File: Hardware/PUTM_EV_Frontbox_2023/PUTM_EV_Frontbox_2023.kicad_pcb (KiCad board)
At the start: 4 copper layers, 75 x 57.9 mm, 251 parts, among them IC1 ELVH-MF12D-HRRJ-C-N3A4, IC2 ELVH-MF12D-HRRJ-C-N3A4, J1 Conn_02x16_Counter_Clockwise, J2 Conn_01x04, K1 UMS05-1A80-75D, Q1 NX7002AK, SW1 Reset switch, U1 STM32G473RCTx, U10 TLP291-4, U11 TLP291-4, U12 MCP2542FDxMF, U13 MCP6001, U14 MCP6N11-005, U15 MCP6001, U16 MCP6N11-005, U17 MCP6002-xMC, U18 MCP6N11-005, U19 TLV743P, U2 MCP6002-xMC, U20 LM4040DBZ-5, U21 MCP6001, U22 MCP6N11-005, U23 MCP6001, U24 MCP6001, U25 MCP6N11-005, U26 MCP6001, U3 IMS330DHCX, U4 TLV743P, U5 TLV743P, U6 BD50FC0FP, U7 LM62440-Q1, U8 MCP2542FDxMF, U9 MCP6N11-005, Y1 ABM8G-48.000MHZ

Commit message: Changed board outline and layout to match ASB
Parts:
- removed J2: Conn_01x04, Connector_PinHeader_2.54mm:PinHeader_1x05_P2.54mm_Vertical
- removed K1: UMS05-1A80-75D, Relay_THT:Relay_StandexMeder_UMS
- added D12: D_Small, Diode_SMD:D_0805_2012Metric_Pad1.15x1.40mm_HandSolder, F.Cu at (190.9, 48.8)
- added H3: MountingHole_Pad, MountingHole:MountingHole_3.2mm_M3_DIN965_Pad_TopBottom, F.Cu at (109.8, 22.1)
- added H4: MountingHole_Pad, MountingHole:MountingHole_3.2mm_M3_DIN965_Pad_TopBottom, F.Cu at (197.8, 22.1)
- added J3: STLINK-V3MINIE, Frontbox:STLINK-V3MINIE, B.Cu at (167.2, 38.8)
- added K2: FINDER-32.21-x000, Relay_THT:Relay_SPDT_Finder_32.21-x000, F.Cu at (190.6, 51.6)
- added R52: 2k, Resistor_SMD:R_0402_1005Metric, F.Cu at (178.6, 61.4)
- added R53: 10k, Resistor_SMD:R_0402_1005Metric, F.Cu at (179.6, 71.0)
- J1: value Conn_02x16_Counter_Clockwise -> Conn_02x15_Counter_Clockwise; footprint Connector_PinHeader_2.54mm:PinHeader_2x16_P2.54mm_Vertical -> Connector_IDC:IDC-Header_2x15-1MP_P2.54mm_Latch6.5mm_Vertical
- moved R20 215.7 mm to (149.1, 71.0)
- moved R21 215.7 mm to (149.1, 69.4)
- moved TP8 215.7 mm to (144.0, 79.3)
- moved C2 215.7 mm to (146.0, 67.9)
- moved C26 215.7 mm to (150.3, 72.8)
- moved D5 215.7 mm to (148.8, 75.2)
- moved R17 215.7 mm to (146.0, 71.0)
- moved R18 215.7 mm to (146.0, 69.4)
- moved R5 215.7 mm to (146.0, 75.2)
- moved R7 215.7 mm to (146.0, 76.7)
- moved TP9 215.7 mm to (145.2, 65.2)
- moved C21 215.7 mm to (149.1, 67.9)
- moved C22 215.7 mm to (149.1, 62.9)
- moved R8 215.7 mm to (149.1, 76.7)
- moved TP6 215.7 mm to (150.1, 79.3)
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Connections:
- C49 pad 1: /APPS1/3V3_POT2 -> /APPS2_3V3
- C50 pad 1: /APPS1/3V3_POT2 -> /APPS2_3V3
- C52 pad 1: /APPS1/DAC_REF2 -> /DAC1_REF
- D10 pad 2: /APPS2/POT1 -> /APPS_POT_2
- D9 pad 2: /APPS1/POT2 -> /APPS_POT_1
- J1 pad 10: /SUSPENSION_POT2_IN -> /APPS2_SHIFTED_GND
- J1 pad 11: /SUSPENSION_POT1_IN -> /APPS1_SHIFTED_3V3
- J1 pad 12: /BRAKE_PRESSURE1_IN -> /APPS2_SHIFTED_3V3
- J1 pad 13: /SAFE-IN -> /LEFT_WHEEL_SC
- J1 pad 14: /SAFE-OUT -> /RIGHT_WHEEL_SC
- J1 pad 15: Net-(J1-Pin_15) -> /OVERTRAVEL
- J1 pad 16: Net-(J1-Pin_16) -> /KILL_PRAWY
- J1 pad 17: Net-(J1-Pin_17) -> /BSPD_SENSE
- J1 pad 18: Net-(J1-Pin_18) -> /SAFE-OUT
- J1 pad 19: /BSPD_SENSE -> /SAFE-IN
- J1 pad 20: /KILL_PRAWY -> /KILL_LEWY
- J1 pad 21: /OVERTRAVEL -> /KILL_KIERA
- J1 pad 22: /KILL_LEWY -> /INERTIA
- J1 pad 23: /KILL_KIERA -> /EBS_SAFETY
- J1 pad 24: /INERTIA -> /CAN2-
- J1 pad 25: /EBS_SAFETY -> /CAN2+
- J1 pad 26: /CAN2- -> /CAN1-
- J1 pad 27: /CAN2+ -> /CAN1+
- J1 pad 28: /CAN1- -> GND
- J1 pad 29: /CAN1+ -> +24V
- J1 pad 3: unconnected-(J1-Pin_3-Pad3) -> /BRAKE_POSITION_IN
- J1 pad 30: GND -> +5V
- J1 pad 4: /BRAKE_POSITION_IN -> /STEERING_POSITION_IN
- J1 pad 5: /STEERING_POSITION_IN -> /BRAKE_PRESSURE1_IN
- J1 pad 6: unconnected-(J1-Pin_6-Pad6) -> /SUSPENSION_POT2_IN
- J1 pad 7: unconnected-(J1-Pin_7-Pad7) -> /SUSPENSION_POT1_IN
- J1 pad 8: unconnected-(J1-Pin_8-Pad8) -> /BRAKE_PRESSURE1_IN
- J1 pad 9: /BRAKE_PRESSURE1_IN -> /APPS1_SHIFTED_GND
- JP3 pad 1: /APPS1/DAC_REF2 -> /DAC1_REF
- R22 pad 1: +5V_EXT -> +5V
- R23 pad 1: +5V_EXT -> +5V
- R29 pad 1: +5V_EXT -> +5V
- R30 pad 1: +5V_EXT -> +5V
- R35 pad 1: +5V_EXT -> +5V
- R36 pad 1: +5V_EXT -> +5V
- R48 pad 2: Net-(J1-Pin_18) -> /APPS2_SHIFTED_3V3
- R5 pad 1: +5V_EXT -> +5V
- R57 pad 2: Net-(J1-Pin_16) -> /APPS2_SHIFTED_GND
- R58 pad 2: Net-(J1-Pin_15) -> /APPS1_SHIFTED_GND
- R6 pad 2: Net-(J1-Pin_17) -> /APPS1_SHIFTED_3V3
- R67 pad 1: /APPS1/3V3_POT2 -> /APPS2_3V3
- R69 pad 1: /APPS1/POT2 -> /APPS_POT_1
- R7 pad 1: +5V_EXT -> +5V
- R70 pad 2: /APPS1/3V3_POT2 -> /APPS2_3V3
- R90 pad 1: /APPS2/POT1 -> /APPS_POT_2
- TP26 pad 1: /APPS1/POT2 -> /APPS_POT_1
- TP30 pad 1: /APPS2/POT1 -> /APPS_POT_2
- U1 pad 10: /Sense_driver -> unconnected-(U1-PC2-Pad10)
- U1 pad 11: /Sense_inertia -> unconnected-(U1-PC3-Pad11)
- U1 pad 2: /Sense_overtravel -> unconnected-(U1-PC13-Pad2)
- U1 pad 4: /Sense_EBS -> unconnected-(U1-PC15-Pad4)
- U1 pad 53: unconnected-(U1-PC11-Pad53) -> /Sense_driver
- U1 pad 54: unconnected-(U1-PC12-Pad54) -> /Sense_right
- U1 pad 55: unconnected-(U1-PD2-Pad55) -> /Sense_inertia
- U1 pad 59: unconnected-(U1-PB6-Pad59) -> /Sense_left
- U1 pad 60: unconnected-(U1-PB7-Pad60) -> /Sense_EBS
- U1 pad 61: unconnected-(U1-PB8-Pad61) -> /Sense_overtravel
- U1 pad 8: /Sense_left -> unconnected-(U1-PC0-Pad8)
- U1 pad 9: /Sense_right -> unconnected-(U1-PC1-Pad9)
- U11 pad 10: /Sense_EBS -> /Safety sense/Sens_Left_Wheel
- U11 pad 11: (no net) -> GND
- U11 pad 12: (no net) -> /Sense_EBS
- U11 pad 5: (no net) -> Net-(R49-Pad2)
- U11 pad 6: (no net) -> GND
- U11 pad 7: Net-(R49-Pad2) -> Net-(R52-Pad2)
- U18 pad 3: /APPS1/POT2 -> /APPS_POT_1
- U18 pad 7: /APPS1/3V3_POT2 -> /APPS2_3V3
- U21 pad 5: /APPS1/3V3_POT2 -> /APPS2_3V3
- U22 pad 3: /APPS2/POT1 -> /APPS_POT_2
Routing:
- net GND: track 101.1 -> 126.3 mm, vias 54 -> 75
- net +5V: track 39.1 -> 59.2 mm, vias 9 -> 21
- net Net-(R92-Pad2): track 5.45 -> 24.5 mm, vias 0 -> 2
- net /APPS1/3V3_POT2: track 18.3 -> 0.00 mm, vias 2 -> 0
- net /APPS2_3V3: track 3.18 -> 21.5 mm, vias 0 -> 2
- net Net-(J1-Pin_17): track 17.3 -> 0.00 mm
- net /APPS_POT_2: track 0.00 -> 17.1 mm, vias 0 -> 2
- net Net-(J1-Pin_15): track 16.2 -> 0.00 mm, vias 1 -> 0
- net /DAC1_REF: track 0.00 -> 15.3 mm
- net /APPS1/DAC_REF2: track 15.3 -> 0.00 mm
- net Net-(J1-Pin_16): track 13.6 -> 0.00 mm, vias 1 -> 0
- net Net-(JP4-C): track 4.85 -> 16.9 mm, vias 0 -> 2
- net Net-(J1-Pin_18): track 10.8 -> 0.00 mm
- net /APPS_sig2: track 5.97 -> 15.9 mm, vias 0 -> 2
- net +5V_EXT: track 9.60 -> 0.00 mm, vias 12 -> 0
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- added copper zone on F.Cu, net +24V
- added copper zone on In1.Cu, net GND
- added copper zone on In2.Cu, net GND
- added copper zone on B.Cu, net Net-(U7-EN)
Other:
- board size 75 x 57.9 mm -> 97 x 70 mm
- rule pad_to_mask_clearance: 0.05 -> 0
- board text removed: "3v3"
- board text removed: "CLK"
- board text removed: "DIO"
- board text removed: "GND"
- board text removed: "NRST"

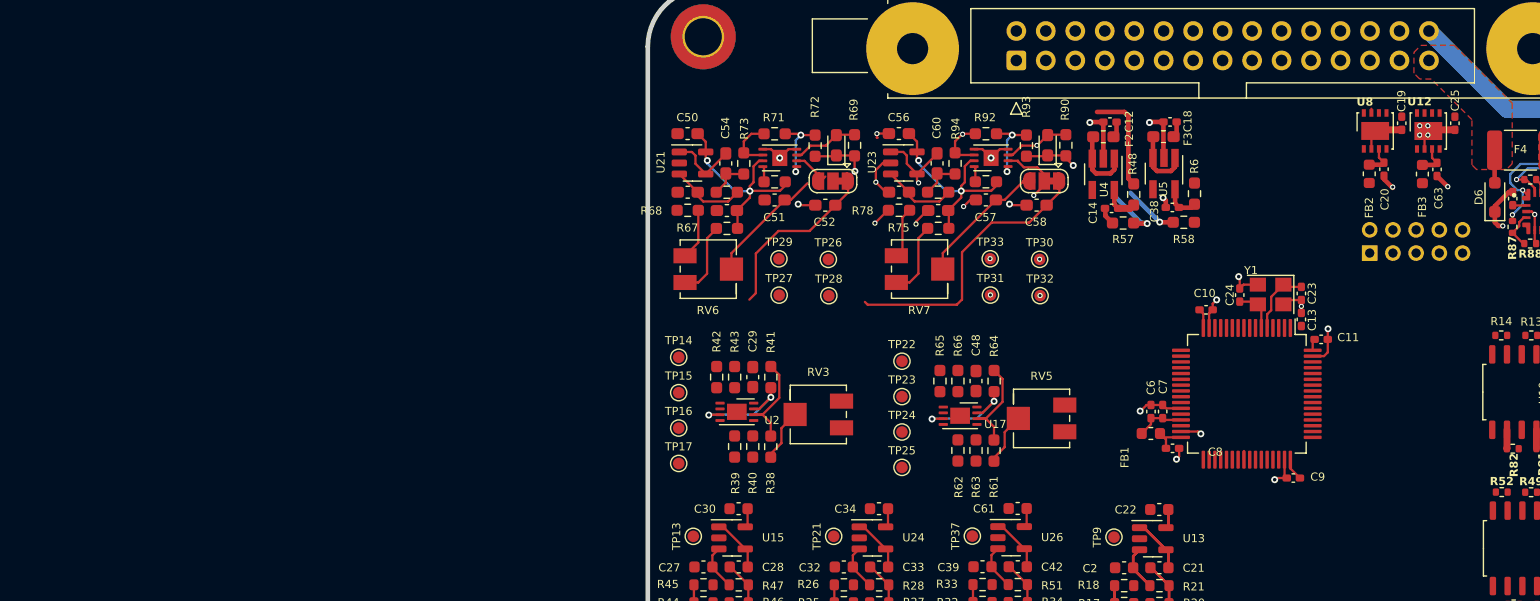
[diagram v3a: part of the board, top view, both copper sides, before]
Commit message: Removed APPS pots
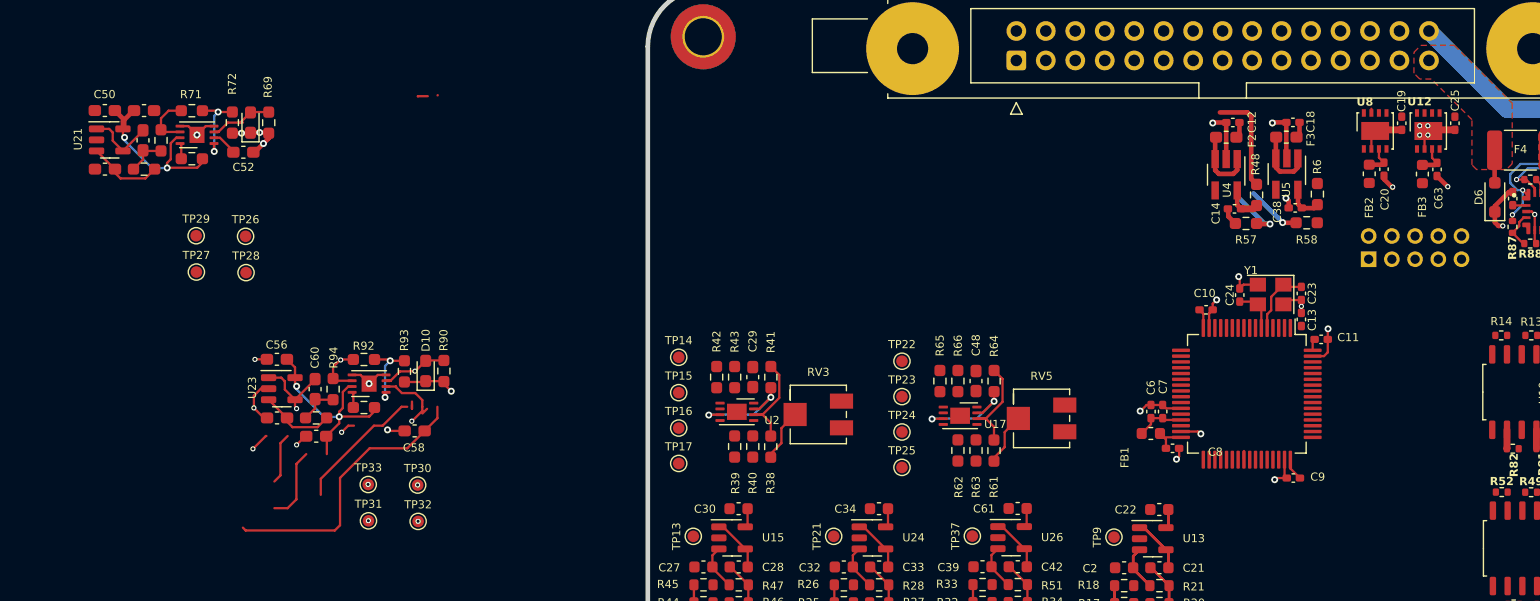
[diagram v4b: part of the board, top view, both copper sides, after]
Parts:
- removed C51, C57: 10n, Capacitor_SMD:C_0603_1608Metric_Pad1.08x0.95mm_HandSolder
- removed JP3, JP4: POT/DAC, Jumper:SolderJumper-3_P1.3mm_Bridged12_RoundedPad1.0x1.5mm
- removed R67, R75: 10k, Resistor_SMD:R_0603_1608Metric_Pad0.98x0.95mm_HandSolder
- removed R68, R78: 33k, Resistor_SMD:R_0603_1608Metric_Pad0.98x0.95mm_HandSolder
- removed RV6, RV7: 1k, Potentiometer_SMD:Potentiometer_Bourns_3214J_Horizontal
- moved C58 57.0 mm to (84.9, 56.1)
- moved C60 57.0 mm to (76.3, 52.5)
- moved R94 57.0 mm to (77.9, 52.5)
- moved TP33 57.0 mm to (80.9, 60.7)
- moved U22 57.0 mm to (81.0, 52.0)
- moved C55 57.0 mm to (76.4, 56.6)
- moved C56 57.0 mm to (73.0, 49.9)
- moved C59 57.0 mm to (73.0, 55.0)
- moved D10 57.0 mm to (85.8, 50.9)
- moved R90 57.0 mm to (87.4, 50.9)
- moved R91 57.0 mm to (80.5, 54.1)
- moved R92 57.0 mm to (80.5, 49.9)
- moved R93 57.0 mm to (84.0, 51.0)
- moved R95 57.0 mm to (76.4, 55.0)
- moved TP30 57.0 mm to (85.1, 60.8)
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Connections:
- TP27 pad 1: Net-(JP3-C) -> /DAC1_REF
- TP31 pad 1: Net-(JP4-C) -> /APPS2/DAC_REF1
- U18 pad 2: Net-(JP3-C) -> /DAC1_REF
- U22 pad 2: Net-(JP4-C) -> /APPS2/DAC_REF1
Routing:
- net (no net): track 0.00 -> 23.2 mm
- net Net-(JP4-C): track 16.9 -> 0.00 mm, vias 2 -> 0
- net /APPS2/DAC_REF1: track 24.2 -> 41.2 mm, vias 0 -> 2
- net /DAC1_REF: track 15.3 -> 2.26 mm
- net Net-(JP4-B): track 12.4 -> 0.00 mm
- net Net-(JP3-B): track 10.4 -> 0.00 mm
- net Net-(R75-Pad2): track 6.47 -> 0.00 mm
- net Net-(R67-Pad2): track 6.47 -> 0.00 mm
- net Net-(JP3-C): track 4.85 -> 0.00 mm
- net Net-(R78-Pad1): track 4.39 -> 0.00 mm
- net Net-(R68-Pad1): track 4.39 -> 0.00 mm
- net GND: track 126.3 -> 128.3 mm, vias 75 -> 76
- net /APPS2_3V3: track 21.5 -> 19.8 mm

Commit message: Routing
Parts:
- removed C40, C5: 100nF, Capacitor_SMD:C_0402_1005Metric_Pad0.74x0.62mm_HandSolder
- removed C59, C60: 100n, Capacitor_SMD:C_0603_1608Metric_Pad1.08x0.95mm_HandSolder
- removed FB4, FB5: 60R@100MHz, Inductor_SMD:L_0603_1608Metric
- removed IC1: ELVH-MF12D-HRRJ-C-N3A4, Frontbox:ELVH005DHRRJINAA4
- removed IC2: ELVH-MF12D-HRRJ-C-N3A4, Frontbox:ELVHL10DHRRDCN2A4
- removed R85, R86: 4k7, Resistor_SMD:R_0402_1005Metric
- removed R90: 100k, Resistor_SMD:R_0603_1608Metric_Pad0.98x0.95mm_HandSolder
- removed R91: 0R, Resistor_SMD:R_0603_1608Metric_Pad0.98x0.95mm_HandSolder
- removed R92, R94, R95: 4k7, Resistor_SMD:R_0603_1608Metric_Pad0.98x0.95mm_HandSolder
- removed R93: 1k, Resistor_SMD:R_0603_1608Metric_Pad0.98x0.95mm_HandSolder
- removed TP4, TP5: TestPoint, TestPoint:TestPoint_Pad_1.0x1.0mm
- added C51: 100n, Capacitor_SMD:C_0603_1608Metric_Pad1.08x0.95mm_HandSolder, F.Cu at (133.2, 31.3)
- added C57: 100n, Capacitor_SMD:C_0603_1608Metric_Pad1.08x0.95mm_HandSolder, F.Cu at (129.8, 36.3)
- added R54: 100k, Resistor_SMD:R_0603_1608Metric_Pad0.98x0.95mm_HandSolder, F.Cu at (143.9, 32.2)
- added R55: 0R, Resistor_SMD:R_0603_1608Metric_Pad0.98x0.95mm_HandSolder, F.Cu at (137.3, 35.5)
- added R56: 4k7, Resistor_SMD:R_0603_1608Metric_Pad0.98x0.95mm_HandSolder, F.Cu at (137.3, 31.3)
- added R59: 1k, Resistor_SMD:R_0603_1608Metric_Pad0.98x0.95mm_HandSolder, F.Cu at (140.8, 32.2)
- added R60: 4k7, Resistor_SMD:R_0603_1608Metric_Pad0.98x0.95mm_HandSolder, F.Cu at (134.6, 33.9)
- added R67: 4k7, Resistor_SMD:R_0603_1608Metric_Pad0.98x0.95mm_HandSolder, F.Cu at (133.2, 36.3)
- C56: value 100n -> 10n
- C58: value 10n -> 100n
- moved C1 163.2 mm to (159.4, -50.4)
- moved SW1 154.0 mm to (152.0, -43.1)
- moved C56 70.4 mm to (141.7, 34.8), turned to 0 degrees
- moved R4 66.4 mm to (159.1, 66.6), turned to 90 degrees
- moved R3 65.7 mm to (160.7, 66.6), turned to 90 degrees
- moved R2 65.1 mm to (162.4, 66.6), turned to 90 degrees
- moved R1 64.6 mm to (164.0, 66.6), turned to 90 degrees
- moved D4 61.7 mm to (159.1, 70.0), turned to -90 degrees
- moved D3 61.0 mm to (160.7, 70.0), turned to -90 degrees
- moved TP32 60.9 mm to (141.3, 40.1)
- moved D2 60.4 mm to (162.4, 70.0), turned to -90 degrees
- moved D1 59.9 mm to (164.0, 70.0), turned to -90 degrees
- moved U22 59.8 mm to (137.7, 33.4)
- moved U23 59.8 mm to (130.2, 33.8)
- moved D10 59.5 mm to (142.4, 32.2)
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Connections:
- C29 pad 1: +3V3 -> +3.3VA
- C48 pad 1: +3V3 -> +3.3VA
- C49 pad 1: /APPS2_3V3 -> /APPS1_3V3
- C50 pad 1: /APPS2_3V3 -> /APPS1_3V3
- C55 pad 1: /APPS2/3V3_POT1 -> /APPS2_3V3
- C56 pad 1: /APPS2/3V3_POT1 -> /DAC2_REF
- C58 pad 1: /APPS2/DAC_REF1 -> Net-(C58-Pad1)
- C58 pad 2: GND -> /APPS_sig2
- J1 pad 18: /SAFE-OUT -> /INERTIA
- J1 pad 19: /SAFE-IN -> /EBS_SAFETY
- J1 pad 22: /INERTIA -> /SAFE-OUT
- J1 pad 23: /EBS_SAFETY -> /SAFE-IN
- J1 pad 24: /CAN2- -> /CAN1-
- J1 pad 25: /CAN2+ -> /CAN1+
- J1 pad 26: /CAN1- -> /CAN2-
- J1 pad 27: /CAN1+ -> /CAN2+
- R70 pad 2: /APPS2_3V3 -> /APPS1_3V3
- TP31 pad 1: /APPS2/DAC_REF1 -> /DAC2_REF
- U17 pad 8: +3V3 -> +3.3VA
- U18 pad 7: /APPS2_3V3 -> /APPS1_3V3
- U2 pad 8: +3V3 -> +3.3VA
- U21 pad 5: /APPS2_3V3 -> /APPS1_3V3
- U22 pad 2: /APPS2/DAC_REF1 -> /DAC2_REF
- U22 pad 7: /APPS2/3V3_POT1 -> /APPS2_3V3
- U23 pad 5: /APPS2/3V3_POT1 -> /APPS2_3V3
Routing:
- net +3.3V: track 8.08 -> 136.1 mm, vias 0 -> 14
- net +5V: track 59.2 -> 167.0 mm, vias 21 -> 26
- net GND: track 128.3 -> 224.7 mm, vias 76 -> 155
- net /APPS2_3V3: track 19.8 -> 109.9 mm, vias 2 -> 12
- net +3.3VA: track 44.2 -> 124.2 mm
- net /APPS1_3V3: track 3.18 -> 59.5 mm, vias 0 -> 2
- net /APPS2/DAC_REF1: track 41.2 -> 0.00 mm, vias 2 -> 0
- net /APPS_POT_2: track 17.1 -> 55.7 mm, vias 2 -> 3
- net Net-(U23-+): track 6.51 -> 39.1 mm
- net Net-(U22-FG): track 6.59 -> 38.1 mm, vias 2 -> 12
- net /APPS_sig2: track 15.8 -> 45.7 mm, vias 2 -> 0
- net /APPS_POT_1: track 6.10 -> 32.5 mm, vias 0 -> 3
- net (no net): track 23.2 -> 0.00 mm
- net /DAC2_REF: track 0.00 -> 23.0 mm
- net Net-(C58-Pad1): track 0.00 -> 21.2 mm
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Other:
- board text removed: "SCL"
- board text removed: "SDA"
